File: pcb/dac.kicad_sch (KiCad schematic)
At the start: 5 parts, among them U3 PCM5102A

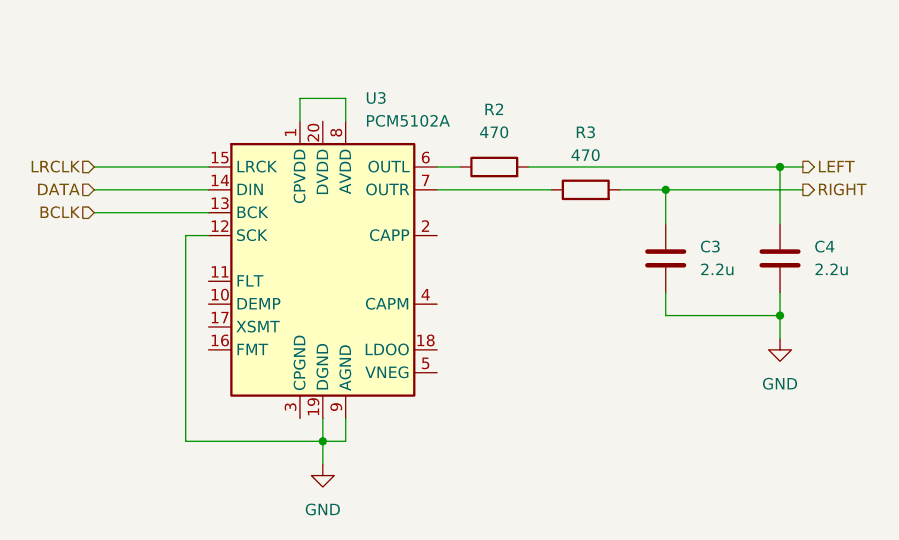
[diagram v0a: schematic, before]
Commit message: Updating schematic based on review from Mike
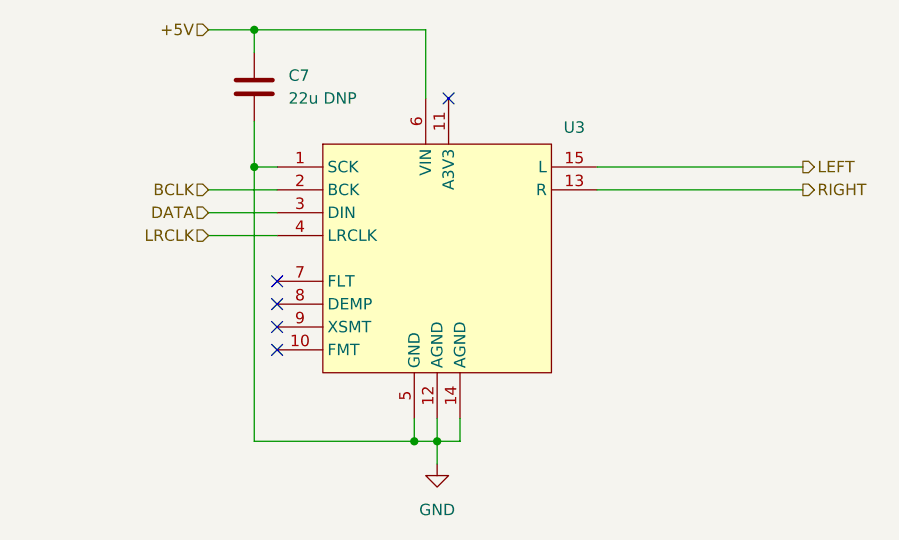
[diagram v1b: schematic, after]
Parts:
- removed C3, C4: 2.2u, symbol Device:C
- removed R2, R3: 470, symbol Device:R
- removed U3: PCM5102A, Package_SO:TSSOP-20_4.4x6.5mm_P0.65mm, symbol Audio:PCM5102A
- added C7: 22u DNP, Capacitor_SMD:C_1206_3216Metric_Pad1.33x1.80mm_HandSolder, symbol Device:C
- added U3: ~, dmxaudio:GY-PCM5102, symbol dmxaudio:PCM5102A_MOD
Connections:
- net BCLK: now also U3.2 (BCK)
- net DATA: now also U3.3 (DIN)
- net GND: now also C7.2, U3.1 (SCK), U3.12 (AGND), U3.14 (AGND), U3.5 (GND)
- net LEFT: now also U3.15 (L)
- net LRCLK: now also U3.4 (LRCLK)
- net RIGHT: now also U3.13 (R)
- new net +5V: C7.1, U3.6 (VIN)
- no-connect marks 0 -> 5
